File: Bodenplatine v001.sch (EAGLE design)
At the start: 113 parts, among them K1 RY612012, K2 RY612012, K3 RY612012, K4 RY612012, K5 RY612012, K6 RY612012, K7 RY612012, K8 RY612012, K9 RY612012, Q1 BC846BLT1SMD, Q2 BC846BLT1SMD, Q3 BC846BLT1SMD, Q4 BC846BLT1SMD, Q5 BC846BLT1SMD, Q6 BC846BLT1SMD, Q7 BC846BLT1SMD, Q8 BC846BLT1SMD, Q9 BC846BLT1SMD, X1 SPRINGCON_AST125_5X2, X10 SPRINGCON_AST125_3X2, X11 SPRINGCON_AST125_4X2, X12 SPRINGCON_AST125_4X2, X13 SPRINGCON_AST125_5X2, X14 236-403, X15 236-402, X2 SPRINGCON_AST125_5X2, X3 SPRINGCON_AST125_5X2, X4 SPRINGCON_AST125_5X2, X5 SPRINGCON_AST125_5X2, X6 SPRINGCON_AST125_5X2, X7 SPRINGCON_AST125_5X2, X8 SPRINGCON_AST125_5X2, X9 SPRINGCON_AST125_5X2

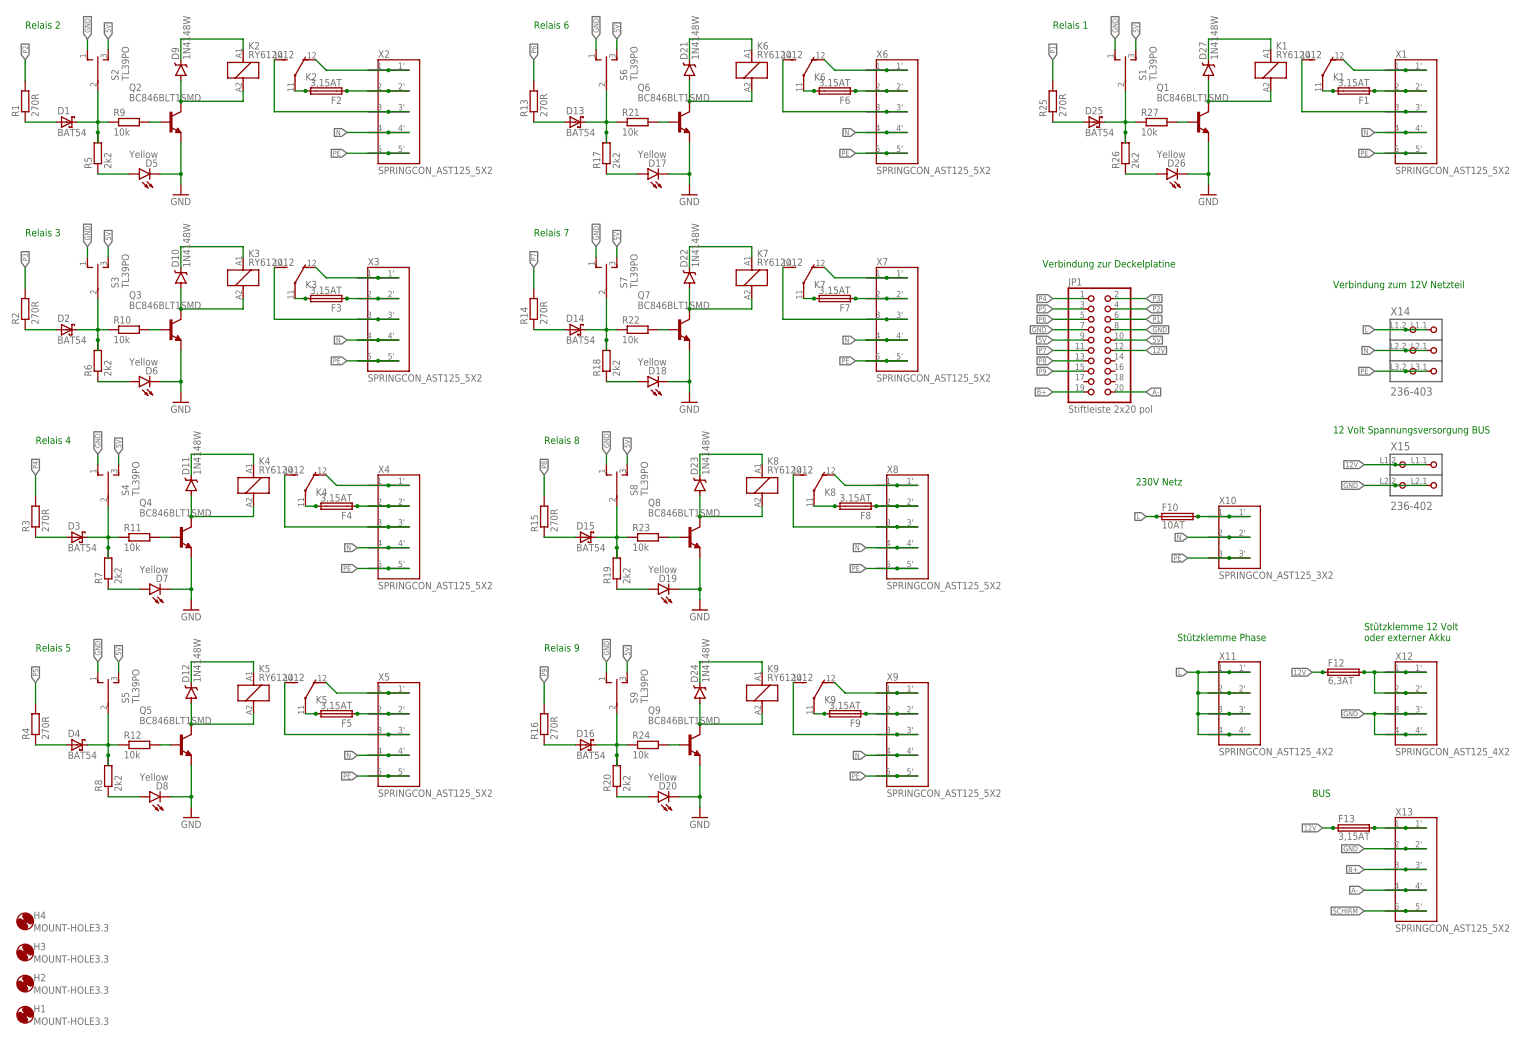
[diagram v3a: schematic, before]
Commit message: BAR43 Diode verbaut und eingebunden
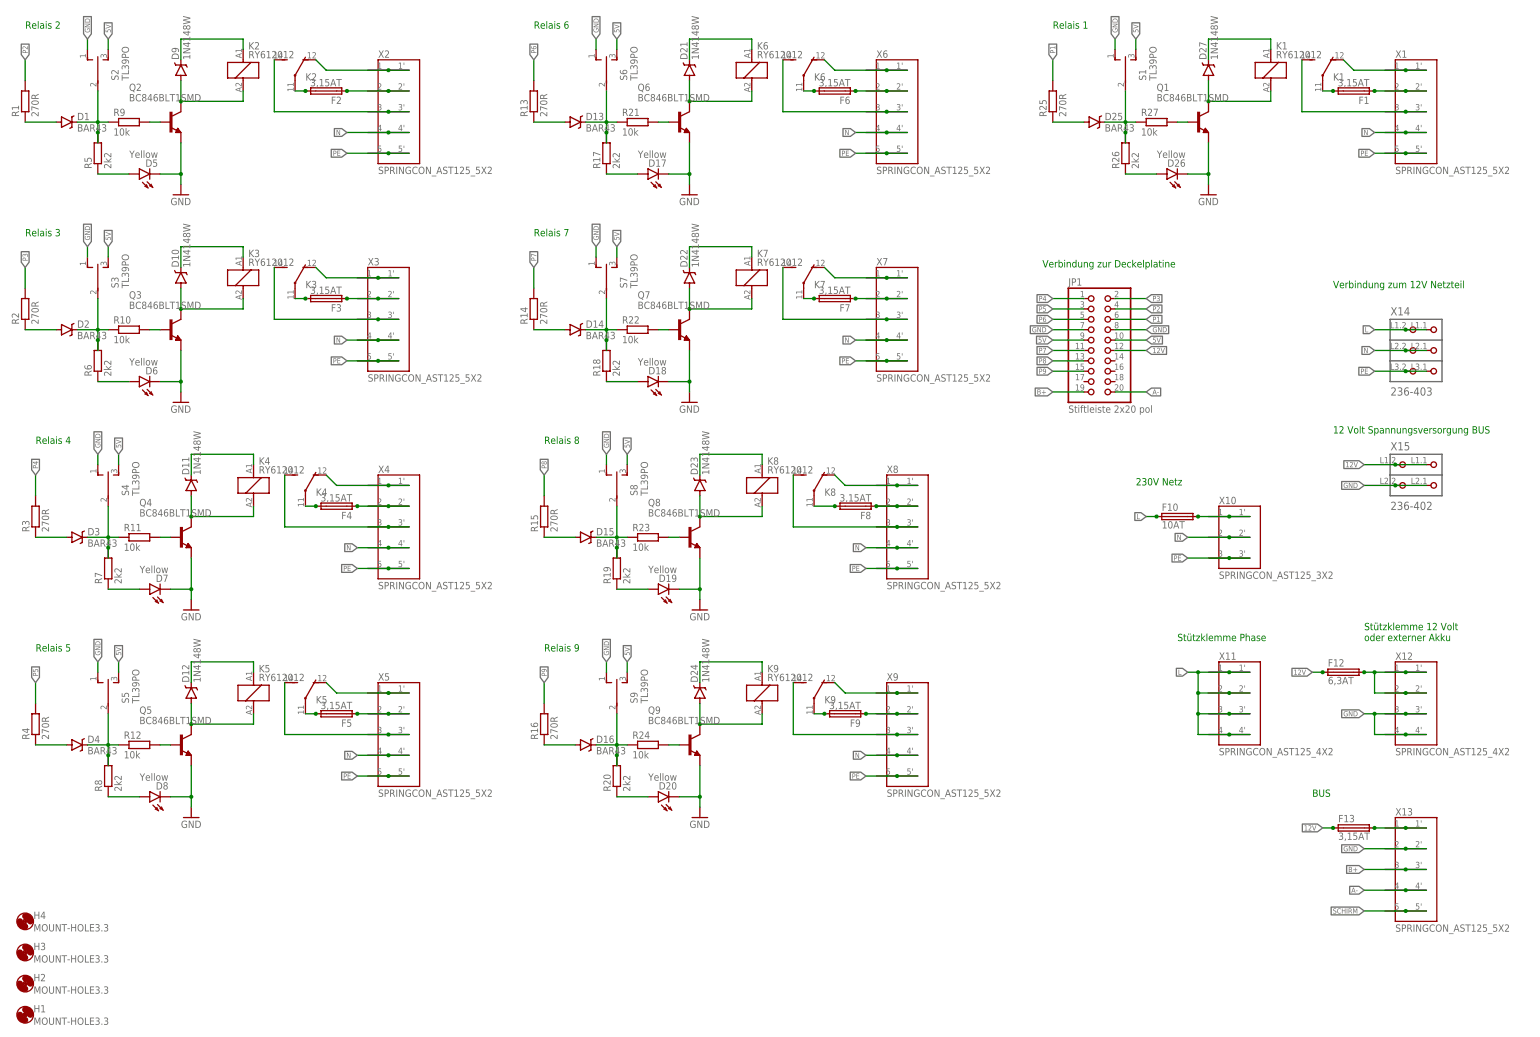
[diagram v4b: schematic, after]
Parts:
- D1, D13, D14, D15, D16, D2, D25, D3, D4: value BAT54 -> BAR43; device diode:BAT54 -> xMZ-Mod-Touch-Bodenplatine:BAR43; MF (none) -> FAIRCHILD SEMICONDUCTOR; MPN (none) -> BAR43; OC_FARNELL unknown -> 2453275
- D10, D11, D12, D21, D22, D23, D24, D27, D9: OC_FARNELL 9549986 -> (none)
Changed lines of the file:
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@@
 <attribute name="OC_FARNELL" value="9334254"/>
 </part>
-<part name="D1" library="diode" deviceset="BAT54" device="">
-<attribute name="MF" value=""/>
-<attribute name="MPN" value=""/>
-<attribute name="OC_FARNELL" value="unknown"/>
+<part name="D1" library="xMZ-Mod-Touch-Bodenplatine" deviceset="BAR43" device="">
+<attribute name="MF" value="FAIRCHILD SEMICONDUCTOR"/>
+<attribute name="MPN" value="BAR43"/>
+<attribute name="OC_FARNELL" value="2453275"/>
 </part>
 <part name="R9" library="rcl" deviceset="R-EU_" device="R0603" value="10k">
@@
 <attribute name="MF" value="VISHAY"/>
 <attribute name="MPN" value="LL4148-GS08"/>
-<attribute name="OC_FARNELL" value="9549986"/>
 </part>
 <part name="F3" library="xMZ-Mod-Touch-Bodenplatine" deviceset="FPG4" device="" value="3,15AT">
@@
 <attribute name="OC_FARNELL" value="9334254"/>
 </part>
-<part name="D2" library="diode" deviceset="BAT54" device="">
-<attribute name="MF" value=""/>
-<attribute name="MPN" value=""/>
-<attribute name="OC_FARNELL" value="unknown"/>
+<part name="D2" library="xMZ-Mod-Touch-Bodenplatine" deviceset="BAR43" device="">
+<attribute name="MF" value="FAIRCHILD SEMICONDUCTOR"/>
+<attribute name="MPN" value="BAR43"/>
+<attribute name="OC_FARNELL" value="2453275"/>
 </part>
 <part name="R10" library="rcl" deviceset="R-EU_" device="R0603" value="10k">
@@
 <attribute name="MF" value="VISHAY"/>
 <attribute name="MPN" value="LL4148-GS08"/>
-<attribute name="OC_FARNELL" value="9549986"/>
 </part>
 <part name="F4" library="xMZ-Mod-Touch-Bodenplatine" deviceset="FPG4" device="" value="3,15AT">
@@
 <attribute name="OC_FARNELL" value="9334254"/>
 </part>
-<part name="D3" library="diode" deviceset="BAT54" device="">
-<attribute name="MF" value=""/>
-<attribute name="MPN" value=""/>
-<attribute name="OC_FARNELL" value="unknown"/>
+<part name="D3" library="xMZ-Mod-Touch-Bodenplatine" deviceset="BAR43" device="">
+<attribute name="MF" value="FAIRCHILD SEMICONDUCTOR"/>
+<attribute name="MPN" value="BAR43"/>
+<attribute name="OC_FARNELL" value="2453275"/>
 </part>
 <part name="R11" library="rcl" deviceset="R-EU_" device="R0603" value="10k">
@@
 <attribute name="MF" value="VISHAY"/>
 <attribute name="MPN" value="LL4148-GS08"/>
-<attribute name="OC_FARNELL" value="9549986"/>
 </part>
 <part name="F5" library="xMZ-Mod-Touch-Bodenplatine" deviceset="FPG4" device="" value="3,15AT">
@@
 <attribute name="OC_FARNELL" value="9334254"/>
 </part>
-<part name="D4" library="diode" deviceset="BAT54" device="">
-<attribute name="MF" value=""/>
-<attribute name="MPN" value=""/>
-<attribute name="OC_FARNELL" value="unknown"/>
+<part name="D4" library="xMZ-Mod-Touch-Bodenplatine" deviceset="BAR43" device="">
+<attribute name="MF" value="FAIRCHILD SEMICONDUCTOR"/>
+<attribute name="MPN" value="BAR43"/>
+<attribute name="OC_FARNELL" value="2453275"/>
 </part>
 <part name="R12" library="rcl" deviceset="R-EU_" device="R0603" value="10k">
@@
 <attribute name="MF" value="VISHAY"/>
 <attribute name="MPN" value="LL4148-GS08"/>
-<attribute name="OC_FARNELL" value="9549986"/>
 </part>
 <part name="F6" library="xMZ-Mod-Touch-Bodenplatine" deviceset="FPG4" device="" value="3,15AT">
@@
 <attribute name="OC_FARNELL" value="9334254"/>
 </part>
-<part name="D13" library="diode" deviceset="BAT54" device="">
-<attribute name="MF" value=""/>
-<attribute name="MPN" value=""/>
-<attribute name="OC_FARNELL" value="unknown"/>
+<part name="D13" library="xMZ-Mod-Touch-Bodenplatine" deviceset="BAR43" device="">
+<attribute name="MF" value="FAIRCHILD SEMICONDUCTOR"/>
+<attribute name="MPN" value="BAR43"/>
+<attribute name="OC_FARNELL" value="2453275"/>
 </part>
 <part name="R21" library="rcl" deviceset="R-EU_" device="R0603" value="10k">
@@
 <attribute name="MF" value="VISHAY"/>
 <attribute name="MPN" value="LL4148-GS08"/>
-<attribute name="OC_FARNELL" value="9549986"/>
 </part>
 <part name="F7" library="xMZ-Mod-Touch-Bodenplatine" deviceset="FPG4" device="" value="3,15AT">
@@
 <attribute name="OC_FARNELL" value="9334254"/>
 </part>
-<part name="D14" library="diode" deviceset="BAT54" device="">
-<attribute name="MF" value=""/>
-<attribute name="MPN" value=""/>
-<attribute name="OC_FARNELL" value="unknown"/>
+<part name="D14" library="xMZ-Mod-Touch-Bodenplatine" deviceset="BAR43" device="">
+<attribute name="MF" value="FAIRCHILD SEMICONDUCTOR"/>
+<attribute name="MPN" value="BAR43"/>
+<attribute name="OC_FARNELL" value="2453275"/>
 </part>
 <part name="R22" library="rcl" deviceset="R-EU_" device="R0603" value="10k">
@@
 <attribute name="MF" value="VISHAY"/>
 <attribute name="MPN" value="LL4148-GS08"/>
-<attribute name="OC_FARNELL" value="9549986"/>
 </part>
 <part name="F8" library="xMZ-Mod-Touch-Bodenplatine" deviceset="FPG4" device="" value="3,15AT">
@@
 <attribute name="OC_FARNELL" value="9334254"/>
 </part>
-<part name="D15" library="diode" deviceset="BAT54" device="">
-<attribute name="MF" value=""/>
-<attribute name="MPN" value=""/>
-<attribute name="OC_FARNELL" value="unknown"/>
+<part name="D15" library="xMZ-Mod-Touch-Bodenplatine" deviceset="BAR43" device="">
+<attribute name="MF" value="FAIRCHILD SEMICONDUCTOR"/>
+<attribute name="MPN" value="BAR43"/>
+<attribute name="OC_FARNELL" value="2453275"/>
 </part>
 <part name="R23" library="rcl" deviceset="R-EU_" device="R0603" value="10k">
@@
 <attribute name="MF" value="VISHAY"/>
 <attribute name="MPN" value="LL4148-GS08"/>
-<attribute name="OC_FARNELL" value="9549986"/>
 </part>
 <part name="F9" library="xMZ-Mod-Touch-Bodenplatine" deviceset="FPG4" device="" value="3,15AT">
@@
 <attribute name="OC_FARNELL" value="9334254"/>
 </part>
-<part name="D16" library="diode" deviceset="BAT54" device="">
-<attribute name="MF" value=""/>
-<attribute name="MPN" value=""/>
-<attribute name="OC_FARNELL" value="unknown"/>
+<part name="D16" library="xMZ-Mod-Touch-Bodenplatine" deviceset="BAR43" device="">
+<attribute name="MF" value="FAIRCHILD SEMICONDUCTOR"/>
+<attribute name="MPN" value="BAR43"/>
+<attribute name="OC_FARNELL" value="2453275"/>
 </part>
 <part name="R24" library="rcl" deviceset="R-EU_" device="R0603" value="10k">
@@
 <attribute name="MF" value="VISHAY"/>
 <attribute name="MPN" value="LL4148-GS08"/>
-<attribute name="OC_FARNELL" value="9549986"/>
 </part>
 <part name="F1" library="xMZ-Mod-Touch-Bodenplatine" deviceset="FPG4" device="" value="3,15AT">
@@
 <attribute name="OC_FARNELL" value="9334254"/>
 </part>
-<part name="D25" library="diode" deviceset="BAT54" device="">
-<attribute name="MF" value=""/>
-<attribute name="MPN" value=""/>
-<attribute name="OC_FARNELL" value="unknown"/>
+<part name="D25" library="xMZ-Mod-Touch-Bodenplatine" deviceset="BAR43" device="">
+<attribute name="MF" value="FAIRCHILD SEMICONDUCTOR"/>
+<attribute name="MPN" value="BAR43"/>
+<attribute name="OC_FARNELL" value="2453275"/>
 </part>
 <part name="R27" library="rcl" deviceset="R-EU_" device="R0603" value="10k">
@@
 <attribute name="MF" value="VISHAY"/>
 <attribute name="MPN" value="LL4148-GS08"/>
-<attribute name="OC_FARNELL" value="9549986"/>
 </part>
 <part name="X12" library="xMZ-Mod-Touch-Bodenplatine" deviceset="SPRINGCON_AST125_4X2" device="">

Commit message: Dioden, Relais und mini Toggle Switch mit Daten von Farnell gefüttert
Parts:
- D1, D13, D14, D15, D16, D2, D25, D3, D4: OC_FARNELL 2453275 -> (none)
- D17, D18, D19, D20, D26, D5, D6, D7, D8: MF (none) -> KINGBRIGHT; MPN (none) -> KP-3216SYC; OC_FARNELL unknown -> 8529990
- K1, K2, K3, K4, K5, K6, K7, K8, K9: MF (none) -> TE CONNECTIVITY / SCHRACK; MPN (none) -> V23061B1005A301; OC_FARNELL (none) -> 1023958
- S1, S2, S3, S4, S5, S6, S7, S8, S9: MF (none) -> TE CONNECTIVITY / ALCOSWITCH; MPN (none) -> A103SYCQ04; OC_FARNELL unknown -> 1818222
